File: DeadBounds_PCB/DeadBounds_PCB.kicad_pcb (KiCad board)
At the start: 2 copper layers, 126 x 108.5 mm, 73 parts, among them J1 Conn_01x04_Socket, J2 Conn_01x04_Socket, J3 Conn_01x06_Socket, J4 Conn_01x04_Socket, J5 Conn_01x05_Socket, SW1 SW_Push, SW2 SW_Push

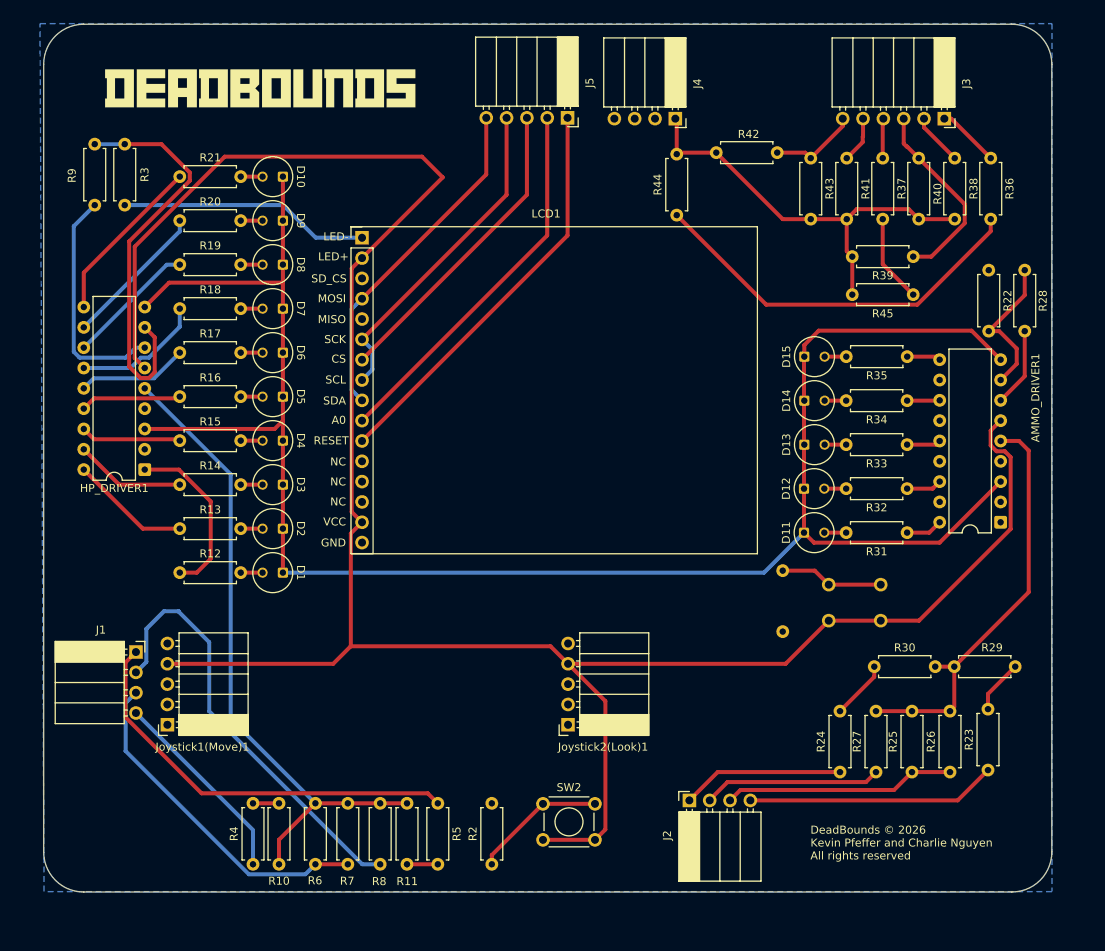
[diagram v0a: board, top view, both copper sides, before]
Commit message: Added amplifier circuit and additional jumpers to PCB
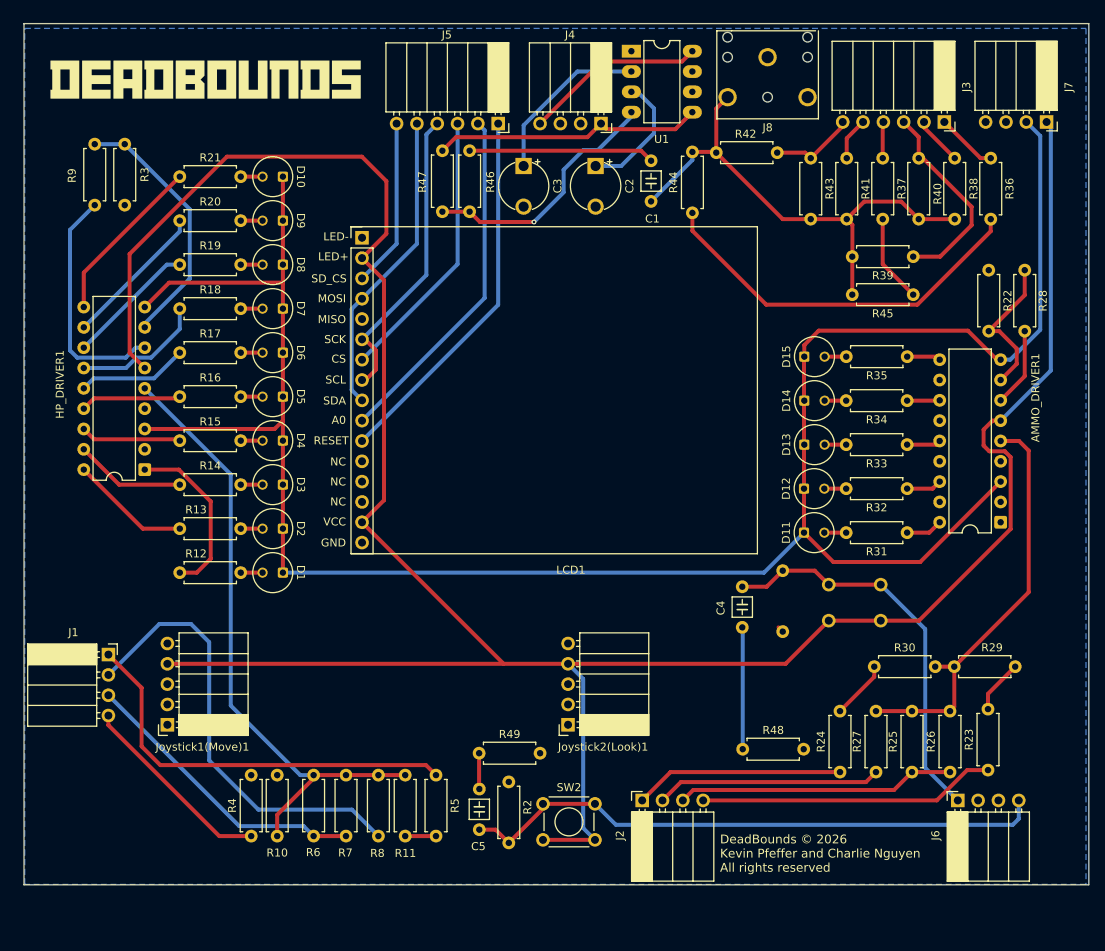
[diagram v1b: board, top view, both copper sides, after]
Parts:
- added C1: 0.1u, ECE319K:C_Axial_200mil, F.Cu at (155.9, 49.6)
- added C2: 1u, ECE319K:CP_Radial_Tantal200mil, F.Cu at (148.9, 50.3)
- added C3: 4.7u, ECE319K:CP_Radial_Tantal200mil, F.Cu at (139.9, 50.3)
- added C4: 0.1u, ECE319K:C_Axial_200mil, F.Cu at (167.3, 102.9)
- added C5: 0.1u, ECE319K:C_Axial_200mil, F.Cu at (134.4, 133.3)
- added J6: Conn_01x04_Socket, Connector_PinSocket_2.54mm:PinSocket_1x04_P2.54mm_Horizontal, F.Cu at (194.2, 129.6)
- added J7: Conn_01x04_Socket, Connector_PinSocket_2.54mm:PinSocket_1x04_P2.54mm_Horizontal, F.Cu at (205.3, 44.8)
- added J8: AudioJack, ECE319K:Jack_3.5mm_CUI_SJ1-3523N_Horizontal, F.Cu at (170.4, 36.7)
- added R46: 20k, Resistor_THT:R_Axial_DIN0207_L6.3mm_D2.5mm_P7.62mm_Horizontal, F.Cu at (133.2, 48.4)
- added R47: 10k, Resistor_THT:R_Axial_DIN0207_L6.3mm_D2.5mm_P7.62mm_Horizontal, F.Cu at (129.8, 48.4)
- added R48: 1.5k, Resistor_THT:R_Axial_DIN0207_L6.3mm_D2.5mm_P7.62mm_Horizontal, F.Cu at (167.3, 123.2)
- added R49: 1.5k, Resistor_THT:R_Axial_DIN0207_L6.3mm_D2.5mm_P7.62mm_Horizontal, F.Cu at (134.4, 123.7)
- added U1: MCP34119P, ECE319K:DIP-8_W7.62mm_LongPads, F.Cu at (153.4, 36.0)
- J5: value Conn_01x05_Socket -> Conn_01x06_Socket; footprint Connector_PinSocket_2.54mm:PinSocket_1x05_P2.54mm_Horizontal -> Connector_PinSocket_2.54mm:PinSocket_1x06_P2.54mm_Horizontal
- moved J4 9.31 mm to (149.6, 45.0)
- moved J5 8.70 mm to (136.8, 45.0)
- moved G*** 6.92 mm to (100.2, 39.3)
- moved J2 5.90 mm to (154.8, 129.6)
- moved R8 3.53 mm to (121.8, 134.1)
- moved R10 3.53 mm to (109.2, 126.4)
- moved R11 3.53 mm to (125.2, 134.1)
- moved R4 3.53 mm to (105.9, 134.1)
- moved R5 3.53 mm to (129.0, 126.4)
- moved R6 3.53 mm to (113.7, 134.1)
- moved R7 3.53 mm to (117.8, 134.1)
- moved J1 3.46 mm to (88.0, 111.4)
- moved R2 3.42 mm to (138.1, 134.9)
- moved R44 1.98 mm to (161.1, 56.2)
- moved J3 0.42 mm to (192.5, 44.8)
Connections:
- net /DAC6/LS1DAC5 renamed /LSDAC5_PB7
- net /LED Bar Drivers + DAC4s/AMMODAC0 renamed /AMMODAC0_PB12
- net /LED Bar Drivers + DAC4s/AMMODAC1 renamed /AMMODAC1_PB13
- J4 pad 4: GND -> Net-(J4-Pin_4)
- LCD1 pad 3: unconnected-(LCD1-SD_CS-Pad3) -> /LCD/SD_CS_LCD
- LCD1 pad 5: unconnected-(LCD1-MISO-Pad5) -> /LCD/MISO_LCD
- R38 pad 2: Net-(J4-Pin_1) -> Net-(J8-tip)
- R39 pad 2: Net-(J4-Pin_1) -> Net-(J8-tip)
- R40 pad 2: Net-(J4-Pin_1) -> Net-(J8-tip)
- R41 pad 2: Net-(J4-Pin_1) -> Net-(J8-tip)
- R42 pad 2: Net-(J4-Pin_1) -> Net-(J8-tip)
- R43 pad 2: Net-(J4-Pin_1) -> Net-(J8-tip)
- R44 pad 2: Net-(J4-Pin_1) -> Net-(J8-tip)
- R45 pad 2: Net-(J4-Pin_1) -> Net-(J8-tip)
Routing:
- net Net-(J8-tip): track 0.00 -> 63.7 mm
- net /SWShoot: track 17.3 -> 74.8 mm
- net +3.3V: track 285.3 -> 324.6 mm
- net /SWLang: track 13.0 -> 49.8 mm
- net +5V: track 231.5 -> 266.7 mm
- net Net-(U1-VIN): track 0.00 -> 31.8 mm, vias 0 -> 1
- net GND: track 31.4 -> 0.75 mm
- net Net-(C1-Pad1): track 0.00 -> 23.2 mm
- net Net-(J4-Pin_4): track 0.00 -> 22.8 mm
- net Net-(U1-FC2): track 0.00 -> 21.3 mm
- net /LCD/SD_CS_LCD: track 0.00 -> 21.1 mm
- net Net-(J4-Pin_1): track 53.5 -> 33.8 mm
- net Net-(HP_DRIVER1-REFADJ): track 51.0 -> 32.3 mm
- net Net-(U1-FC1): track 0.00 -> 15.8 mm
- net Net-(C4-Pad2): track 0.00 -> 15.3 mm
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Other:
- board size 126 x 108.5 mm -> 133.1 x 107.7 mm

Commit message: Added mounting holes and rerouted around joystick. PCB Ordered
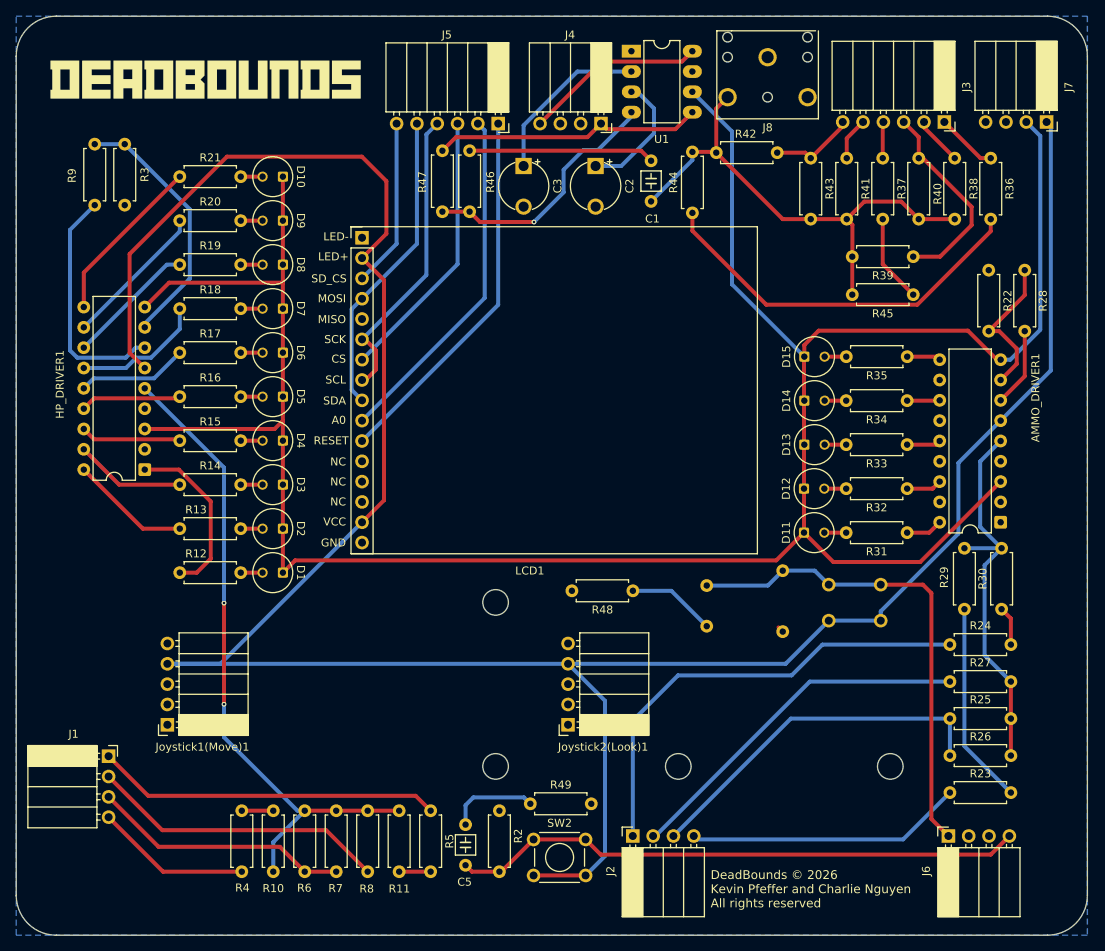
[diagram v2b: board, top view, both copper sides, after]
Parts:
- added REF**: MountingHole_3.2mm_M3, MountingHole:MountingHole_3.2mm_M3, F.Cu at (185.8, 125.3)
- added REF**: MountingHole_3.2mm_M3, MountingHole:MountingHole_3.2mm_M3, F.Cu at (159.3, 125.3)
- added REF**: MountingHole_3.2mm_M3, MountingHole:MountingHole_3.2mm_M3, F.Cu at (136.4, 125.3)
- added REF**: MountingHole_3.2mm_M3, MountingHole:MountingHole_3.2mm_M3, F.Cu at (136.4, 104.8)
- C4: moved to B.Cu
- moved R48 24.1 mm to (153.6, 103.4), turned to 180 degrees
- moved R24 21.0 mm to (193.2, 110.1), turned to 0 degrees
- moved R30 17.5 mm to (199.7, 105.7), turned to 90 degrees
- moved R27 14.6 mm to (193.2, 114.8), turned to 0 degrees
- moved J1 12.7 mm to (88.1, 124.1)
- moved R29 9.59 mm to (195.1, 105.7), turned to 90 degrees
- moved R49 9.00 mm to (140.8, 130.0)
- moved R25 8.19 mm to (193.2, 119.4), turned to 0 degrees
- moved R23 5.53 mm to (193.2, 128.6), turned to 0 degrees
- moved C5 4.77 mm to (132.7, 137.7)
- moved R8 4.65 mm to (120.5, 138.5)
- moved R7 4.62 mm to (116.5, 138.5)
- moved J2 4.60 mm to (153.6, 134.1)
- moved J6 4.60 mm to (193.1, 134.1)
- moved SW2 4.60 mm to (141.2, 134.5)
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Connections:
- J5 pad 3: /LCD/CS_LCD -> /SD_CS
- J5 pad 6: /LCD/SD_CS_LCD -> /SD_CS
- LCD1 pad 3: /LCD/SD_CS_LCD -> /SD_CS
- LCD1 pad 7: /LCD/CS_LCD -> /SD_CS
- U1 pad 6: unconnected-(U1-Vcc-Pad6) -> +5V
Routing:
- net /SD_CS: track 0.00 -> 55.6 mm
- net +5V: track 266.7 -> 305.6 mm
- net /LCD/CS_LCD: track 34.5 -> 0.00 mm
- net /AMMODAC0_PB12: track 26.2 -> 58.0 mm
- net /LCD/SD_CS_LCD: track 21.1 -> 0.00 mm
- net /LED Bar Drivers + DAC4s/HPDAC1: track 56.0 -> 37.3 mm
- net Net-(R23-Pad2): track 6.72 -> 25.3 mm
- net /AMMODAC1_PB13: track 28.2 -> 45.1 mm
- net /SWLang: track 49.8 -> 61.3 mm
- net /LED Bar Drivers + DAC4s/AMMODAC2: track 34.9 -> 45.3 mm
- net /LED Bar Drivers + DAC4s/HPDAC0: track 51.5 -> 43.1 mm
- net Net-(C5-Pad2): track 4.49 -> 11.3 mm
- net /LED Bar Drivers + DAC4s/HPDAC3: track 24.8 -> 19.5 mm
- net +3.3V: track 324.6 -> 329.9 mm
- net /LED Bar Drivers + DAC4s/HPDAC2: track 37.0 -> 32.3 mm
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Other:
- board size 133.1 x 107.7 mm -> 133.9 x 114.9 mm
